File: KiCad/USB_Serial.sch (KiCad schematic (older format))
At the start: 0 parts

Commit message: Updating changes
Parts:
- added C?: 100n, symbol Device:C
- added C? (x2): 22p, symbol Device:C
- added D? (x2): YELLOW, symbol Device:LED
- added J?: USB_B_Micro, symbol Connector:USB_B_Micro
- added J?: AVR-ISP-6, symbol Connector:AVR-ISP-6
- added R? (x2): 22R, symbol Device:R
- added R? (x4): 1k, symbol Device:R
- added R? (x3): R, symbol Device:R
- added R?: 1M, symbol Device:R
- added U?: ATmega8U2-AU, Package_QFP:TQFP-32_7x7mm_P0.8mm, symbol MCU_Microchip_ATmega:ATmega8U2-AU
- added Y?: Crystal, symbol Device:Crystal
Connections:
- net labels added: +5V, GND, MISO, MOSI, SCK, USBVCC, ~RESET
- wire segments 0 -> 47
- no-connect marks 0 -> 8

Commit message: first stab at changes, added switching power supply, updated 2 ATmega footprints per KiCAD 5.0.2 update
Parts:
- U?: symbol MCU_Microchip_ATmega:ATmega8U2-AU -> Snack-Machine-rescue:ATmega8U2-AU-MCU_Microchip_ATmega
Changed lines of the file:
@@
 TX_USB
 $Comp
-L MCU_Microchip_ATmega:ATmega8U2-AU U?
+L Snack-Machine-rescue:ATmega8U2-AU-MCU_Microchip_ATmega U?
 U 1 1 5BC6B5AA
 P 4900 2800

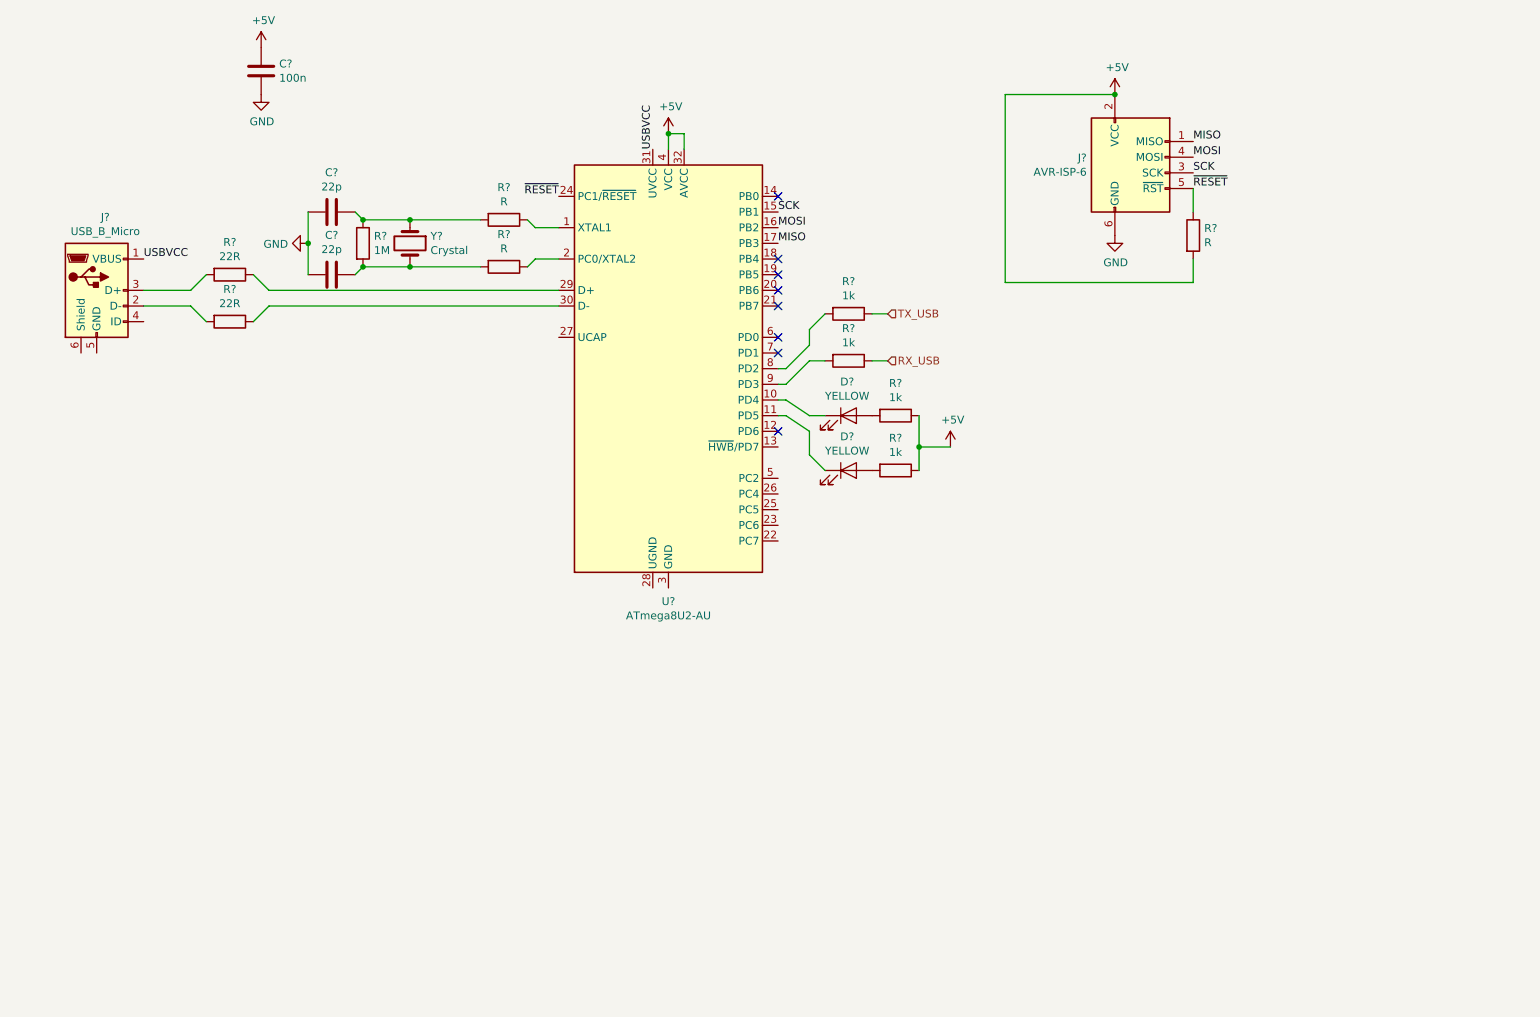
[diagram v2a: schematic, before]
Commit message: Large number of changes, some cosmetic, most functional. Added analog current sense circuit, added switching power supply (24V->5V), added switch connector for sensing when door is open, added LCD12864 connectors, added RFID125kHz connectors, modified multi-drop bus connection, updated bootloader hardware to match Arduino MEGA R3 circuit, plus other small changes.
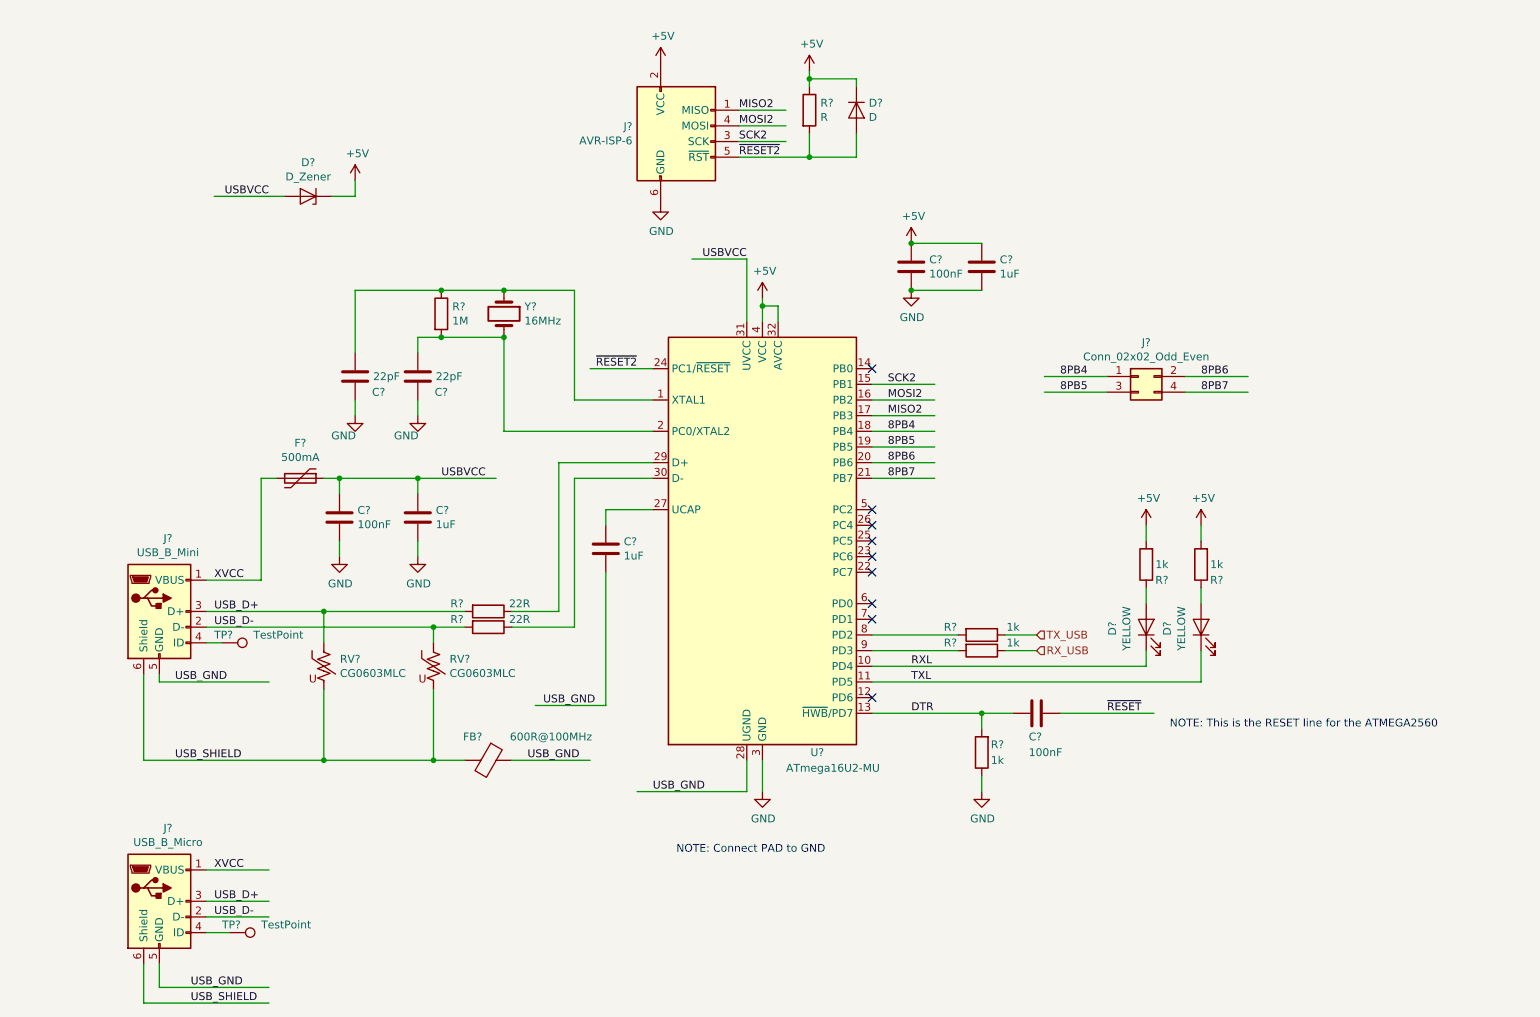
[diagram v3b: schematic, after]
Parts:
- removed J?: USB_B_Micro, symbol Connector:USB_B_Micro
- removed R? (x2): R, symbol Device:R
- removed U?: ATmega8U2-AU, Package_QFP:TQFP-32_7x7mm_P0.8mm, symbol Snack-Machine-rescue:ATmega8U2-AU-MCU_Microchip_ATmega
- added C? (x3): 1uF, symbol Device:C
- added C? (x2): 100nF, symbol Device:C
- added D?: D, Diodes_SMD:D_1206, symbol Device:D
- added D?: D_Zener, Diodes_SMD:D_SMB_Handsoldering, symbol Device:D_Zener
- added F?: 500mA, symbol Device:Polyfuse
- added FB?: 600R@100MHz, Inductors_SMD:L_0603_HandSoldering, symbol Device:Ferrite_Bead
- added J?: USB_B_Mini, Connectors:USB_Mini-B, symbol Connector:USB_B_Mini
- added J?: USB_B_Micro, symbol Connector:USB_B_Micro
- added J?: Conn_02x02_Odd_Even, symbol Connector_Generic:Conn_02x02_Odd_Even
- added R?: 1k, symbol Device:R
- added RV? (x2): CG0603MLC, Resistors_SMD:R_0603_HandSoldering, symbol Device:Varistor_US
- added TP? (x2): TestPoint, symbol Connector:TestPoint
- added U?: ATmega16U2-MU, Package_DFN_QFN:QFN-32-1EP_5x5mm_P0.5mm_EP3.1x3.1mm, symbol MCU_Microchip_ATmega:ATmega16U2-MU
- C?: value 100n -> 100nF
- C? (x2): value 22p -> 22pF
- Y?: value Crystal -> 16MHz
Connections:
- net labels added: 8PB4, 8PB5, 8PB6, 8PB7, DTR, MISO2, MOSI2, RXL, SCK2, TXL, USB_D+, USB_D-, USB_GND, USB_SHIELD, XVCC, ~RESET2
- net labels removed: MISO, MOSI, SCK
- wire segments 47 -> 111
- no-connect marks 8 -> 9
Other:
- note added: "NOTE: Connect PAD to GND"
- note added: "NOTE: This is the RESET line for the ATMEGA2560"
- moved on the sheet: C?, D?, J?, R?, Y?

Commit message: small tweaks
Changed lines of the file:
@@
 NoConn ~ 6200 4400
 NoConn ~ 6200 4900
-Text Notes 8100 5100 0    50   ~ 0
+Text Notes 8100 5150 0    50   ~ 0
 NOTE: This is the RESET line for the ATMEGA2560
 Wire Wire Line
@@
 Wire Wire Line
 	5500 2350 5500 2400
+Text HLabel 8000 5000 2    50   Input ~ 0
+~RESET
 $EndSCHEMATC

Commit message: Updating annotations for all schematics
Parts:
- gave numbers to parts that had none: 33

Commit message: latest changes, mostly test points and annotations
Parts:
- removed Y2: 16MHz, symbol Device:Crystal
- added Y2: 16MHz, symbol Device:Crystal_GND2
- renumbered C15 to C21, C16 to C22, C17 to C23, C18 to C24, C19 to C25, C20 to C26, C21 to C27, C22 to C28, R49 to R55, R50 to R56, R51 to R57, R52 to R58, R53 to R59, R54 to R60, R55 to R61, R56 to R62, R57 to R63, TP11 to TP53, TP12 to TP54
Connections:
- wire segments 111 -> 116
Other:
- moved on the sheet: C23, C24, R56

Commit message: Updating components and footprints
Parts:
- C17: renamed from C23; footprint (none) -> Capacitor_SMD:C_0603_1608Metric_Pad1.05x0.95mm_HandSolder
- C18: renamed from C24; footprint (none) -> Capacitor_SMD:C_0603_1608Metric_Pad1.05x0.95mm_HandSolder
- C21, C22, C25, C26, C27, C28: footprint (none) -> Capacitor_SMD:C_0603_1608Metric_Pad1.05x0.95mm_HandSolder
- D5, D6: footprint (none) -> LED_SMD:LED_0603_1608Metric_Pad1.05x0.95mm_HandSolder
- J14: footprint (none) -> Connector_PinHeader_1.00mm:PinHeader_2x03_P1.00mm_Vertical_SMD
- R50: renamed from R56; footprint (none) -> Resistor_SMD:R_0603_1608Metric_Pad1.05x0.95mm_HandSolder
- R55, R57, R58, R59, R60, R61, R62, R63: footprint (none) -> Resistor_SMD:R_0603_1608Metric_Pad1.05x0.95mm_HandSolder
- TP53, TP54: footprint (none) -> TestPoint:TestPoint_THTPad_D1.0mm_Drill0.5mm
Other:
- moved on the sheet: R50
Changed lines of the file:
@@
 F 0 "R59" V 3700 4150 50  0000 C CNN
 F 1 "22R" V 3700 4550 50  0000 C CNN
-F 2 "" V 3680 4350 50  0001 C CNN
+F 2 "Resistor_SMD:R_0603_1608Metric_Pad1.05x0.95mm_HandSolder" V 3680 4350 50  0001 C CNN
 F 3 "~" H 3750 4350 50  0001 C CNN
 	1    3750 4350
@@
 F 0 "R60" V 3700 4250 50  0000 C CNN
 F 1 "22R" V 3700 4650 50  0000 C CNN
-F 2 "" V 3680 4450 50  0001 C CNN
+F 2 "Resistor_SMD:R_0603_1608Metric_Pad1.05x0.95mm_HandSolder" V 3680 4450 50  0001 C CNN
 F 3 "~" H 3750 4450 50  0001 C CNN
 	1    3750 4450
@@
 F 0 "C21" H 6565 2196 50  0000 L CNN
 F 1 "100nF" H 6565 2105 50  0000 L CNN
-F 2 "" H 6488 2000 50  0001 C CNN
+F 2 "Capacitor_SMD:C_0603_1608Metric_Pad1.05x0.95mm_HandSolder" H 6488 2000 50  0001 C CNN
 F 3 "~" H 6450 2150 50  0001 C CNN
 	1    6450 2150
@@
 F 0 "R61" V 6850 4300 50  0000 C CNN
 F 1 "1k" V 6850 4700 50  0000 C CNN
-F 2 "" V 6830 4500 50  0001 C CNN
+F 2 "Resistor_SMD:R_0603_1608Metric_Pad1.05x0.95mm_HandSolder" V 6830 4500 50  0001 C CNN
 F 3 "~" H 6900 4500 50  0001 C CNN
 	1    6900 4500
@@
 F 0 "R62" V 6850 4400 50  0000 C CNN
 F 1 "1k" V 6850 4800 50  0000 C CNN
-F 2 "" V 6830 4600 50  0001 C CNN
+F 2 "Resistor_SMD:R_0603_1608Metric_Pad1.05x0.95mm_HandSolder" V 6830 4600 50  0001 C CNN
 F 3 "~" H 6900 4600 50  0001 C CNN
 	1    6900 4600
@@
 F 0 "D5" H 7941 4666 50  0000 C CNN
 F 1 "YELLOW" H 7941 4575 50  0000 C CNN
-F 2 "" H 7950 4450 50  0001 C CNN
+F 2 "LED_SMD:LED_0603_1608Metric_Pad1.05x0.95mm_HandSolder" H 7950 4450 50  0001 C CNN
 F 3 "~" H 7950 4450 50  0001 C CNN
 	1    7950 4450
@@
 F 0 "D6" H 8291 4666 50  0000 C CNN
 F 1 "YELLOW" H 8291 4575 50  0000 C CNN
-F 2 "" H 8300 4450 50  0001 C CNN
+F 2 "LED_SMD:LED_0603_1608Metric_Pad1.05x0.95mm_HandSolder" H 8300 4450 50  0001 C CNN
 F 3 "~" H 8300 4450 50  0001 C CNN
 	1    8300 4450
@@
 F 0 "R57" H 7850 4150 50  0000 C CNN
 F 1 "1k" H 7850 4050 50  0000 C CNN
-F 2 "" V 7880 4050 50  0001 C CNN
+F 2 "Resistor_SMD:R_0603_1608Metric_Pad1.05x0.95mm_HandSolder" V 7880 4050 50  0001 C CNN
 F 3 "~" H 7950 4050 50  0001 C CNN
 	1    7950 4050
@@
 F 0 "R58" H 8200 4150 50  0000 C CNN
 F 1 "1k" H 8200 4050 50  0000 C CNN
-F 2 "" V 8230 4050 50  0001 C CNN
+F 2 "Resistor_SMD:R_0603_1608Metric_Pad1.05x0.95mm_HandSolder" V 8230 4050 50  0001 C CNN
 F 3 "~" H 8300 4050 50  0001 C CNN
 	1    8300 4050
@@
 F 0 "J14" H 4670 1446 50  0000 R CNN
 F 1 "AVR-ISP-6" H 4670 1355 50  0000 R CNN
-F 2 "" V 4700 1400 50  0001 C CNN
+F 2 "Connector_PinHeader_1.00mm:PinHeader_2x03_P1.00mm_Vertical_SMD" V 4700 1400 50  0001 C CNN
 F 3 " ~" H 3675 800 50  0001 C CNN
 	1    4950 1350
@@
 F 0 "R55" H 5870 1196 50  0000 L CNN
 F 1 "R" H 5870 1105 50  0000 L CNN
-F 2 "" V 5730 1150 50  0001 C CNN
+F 2 "Resistor_SMD:R_0603_1608Metric_Pad1.05x0.95mm_HandSolder" V 5730 1150 50  0001 C CNN
 F 3 "~" H 5800 1150 50  0001 C CNN
 	1    5800 1150
@@
 ~RESET2
 $Comp
-L Device:R R56
+L Device:R R50
 U 1 1 5BC6CF74
-P 3250 2450
-F 0 "R56" H 3320 2496 50  0000 L CNN
-F 1 "1M" H 3320 2405 50  0000 L CNN
-F 2 "" V 3180 2450 50  0001 C CNN
-F 3 "~" H 3250 2450 50  0001 C CNN
-	1    3250 2450
-	1    0    0    -1
-$EndComp
-$Comp
-L Device:C C23
+P 3200 2450
+F 0 "R50" H 3270 2496 50  0000 L CNN
+F 1 "1M" H 3270 2405 50  0000 L CNN
+F 2 "Resistor_SMD:R_0603_1608Metric_Pad1.05x0.95mm_HandSolder" V 3130 2450 50  0001 C CNN
+F 3 "~" H 3200 2450 50  0001 C CNN
+	1    3200 2450
+	1    0    0    -1
+$EndComp
+$Comp
+L Device:C C17
 U 1 1 5BC6D8E3
 P 2700 2850
-F 0 "C23" H 2550 2950 50  0000 C CNN
+F 0 "C17" H 2550 2950 50  0000 C CNN
 F 1 "22pF" H 2500 2850 50  0000 C CNN
-F 2 "" H 2738 2700 50  0001 C CNN
+F 2 "Capacitor_SMD:C_0603_1608Metric_Pad1.05x0.95mm_HandSolder" H 2738 2700 50  0001 C CNN
 F 3 "~" H 2700 2850 50  0001 C CNN
 	1    2700 2850
@@
 $EndComp
 $Comp
-L Device:C C24
+L Device:C C18
 U 1 1 5BC6D985
 P 3100 2850
-F 0 "C24" H 2950 2950 50  0000 C CNN
+F 0 "C18" H 2950 2950 50  0000 C CNN
 F 1 "22pF" H 2900 2850 50  0000 C CNN
-F 2 "" H 3138 2700 50  0001 C CNN
+F 2 "Capacitor_SMD:C_0603_1608Metric_Pad1.05x0.95mm_HandSolder" H 3138 2700 50  0001 C CNN
 F 3 "~" H 3100 2850 50  0001 C CNN
 	1    3100 2850
 	-1   0    0    1
 $EndComp
-Connection ~ 3250 2600
-Connection ~ 3250 2300
 $Comp
 L Device:C C22
@@
 F 0 "C22" H 7015 2196 50  0000 L CNN
 F 1 "1uF" H 7015 2105 50  0000 L CNN
-F 2 "" H 6938 2000 50  0001 C CNN
+F 2 "Capacitor_SMD:C_0603_1608Metric_Pad1.05x0.95mm_HandSolder" H 6938 2000 50  0001 C CNN
 F 3 "~" H 6900 2150 50  0001 C CNN
 	1    6900 2150
@@
 	6900 2300 6450 2300
 Connection ~ 6450 2300
-Wire Wire Line
-	3250 2300 3850 2300
-Wire Wire Line
-	3250 2600 3650 2600
-Wire Wire Line
-	3250 2300 2700 2300
-Wire Wire Line
-	3250 2600 3100 2600
 Wire Wire Line
 	5350 1450 5800 1450
@@
 F 0 "R63" H 6800 5200 50  0000 C CNN
 F 1 "1k" H 6800 5300 50  0000 C CNN
-F 2 "" V 6830 5250 50  0001 C CNN
+F 2 "Resistor_SMD:R_0603_1608Metric_Pad1.05x0.95mm_HandSolder" V 6830 5250 50  0001 C CNN
 F 3 "~" H 6900 5250 50  0001 C CNN
 	1    6900 5250
@@
 F 0 "C28" V 7400 4950 50  0000 L CNN
 F 1 "100nF" V 7500 4950 50  0000 L CNN
-F 2 "" H 7288 4850 50  0001 C CNN
+F 2 "Capacitor_SMD:C_0603_1608Metric_Pad1.05x0.95mm_HandSolder" H 7288 4850 50  0001 C CNN
 F 3 "~" H 7250 5000 50  0001 C CNN
 	1    7250 5000
@@
 F 0 "TP54" V 2050 6350 50  0000 L CNN
 F 1 "TestPoint" V 2050 6600 50  0000 L CNN
-F 2 "" H 2300 6400 50  0001 C CNN
+F 2 "TestPoint:TestPoint_THTPad_D1.0mm_Drill0.5mm" H 2300 6400 50  0001 C CNN
 F 3 "~" H 2300 6400 50  0001 C CNN
 	1    2100 6400
@@
 F 0 "TP53" V 2000 4500 50  0000 L CNN
 F 1 "TestPoint" V 2000 4750 50  0000 L CNN
-F 2 "" H 2250 4550 50  0001 C CNN
+F 2 "TestPoint:TestPoint_THTPad_D1.0mm_Drill0.5mm" H 2250 4550 50  0001 C CNN
 F 3 "~" H 2250 4550 50  0001 C CNN
 	1    2050 4550
@@
 F 0 "C25" H 2915 3796 50  0000 L CNN
 F 1 "100nF" H 2915 3705 50  0000 L CNN
-F 2 "" H 2838 3600 50  0001 C CNN
+F 2 "Capacitor_SMD:C_0603_1608Metric_Pad1.05x0.95mm_HandSolder" H 2838 3600 50  0001 C CNN
 F 3 "~" H 2800 3750 50  0001 C CNN
 	1    2800 3750
@@
 F 0 "C26" H 3415 3796 50  0000 L CNN
 F 1 "1uF" H 3415 3705 50  0000 L CNN
-F 2 "" H 3338 3600 50  0001 C CNN
+F 2 "Capacitor_SMD:C_0603_1608Metric_Pad1.05x0.95mm_HandSolder" H 3338 3600 50  0001 C CNN
 F 3 "~" H 3300 3750 50  0001 C CNN
 	1    3300 3750
@@
 F 0 "C27" H 4615 3996 50  0000 L CNN
 F 1 "1uF" H 4615 3905 50  0000 L CNN
-F 2 "" H 4538 3800 50  0001 C CNN
+F 2 "Capacitor_SMD:C_0603_1608Metric_Pad1.05x0.95mm_HandSolder" H 4538 3800 50  0001 C CNN
 F 3 "~" H 4500 3950 50  0001 C CNN
 	1    4500 3950
@@
 Wire Wire Line
 	3550 2450 3550 2700
+Wire Wire Line
+	2700 2300 3200 2300
+Wire Wire Line
+	3100 2600 3200 2600
+Connection ~ 3200 2300
+Wire Wire Line
+	3200 2300 3850 2300
+Connection ~ 3200 2600
+Wire Wire Line
+	3200 2600 3650 2600
 $EndSCHEMATC
